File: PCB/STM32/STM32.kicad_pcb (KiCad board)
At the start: 2 copper layers, 41 x 38 mm, 47 parts, among them J18 St-Link, J2 St-Link, SW1 SW_Push, U1 LTV-356T, U2 MIC5205-5.0YM5, U3 STM32F411RETx, U4 MCP1703A-3302_SOT23, Y1 16MHz

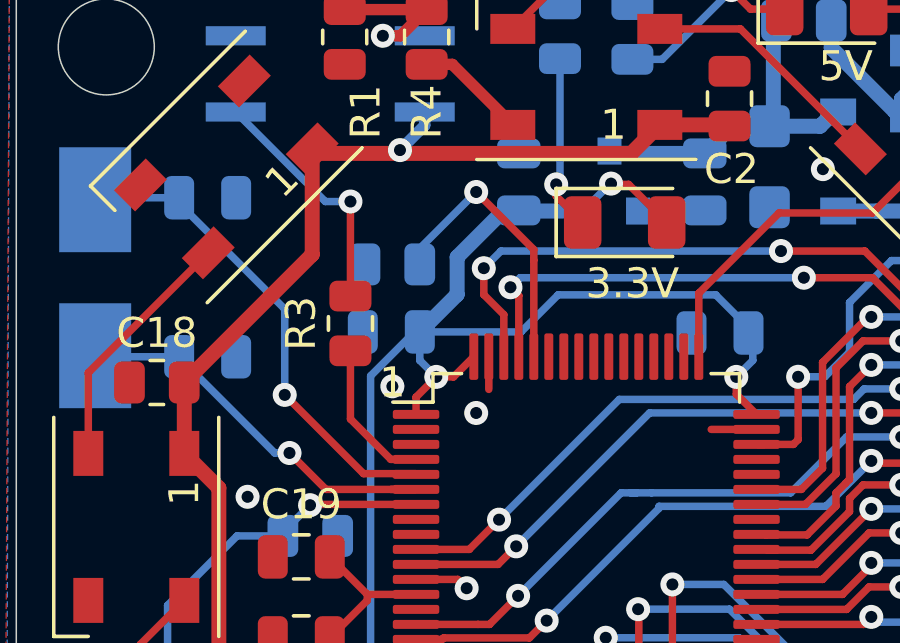
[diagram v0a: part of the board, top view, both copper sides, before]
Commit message: Changed NeoPixel output pin
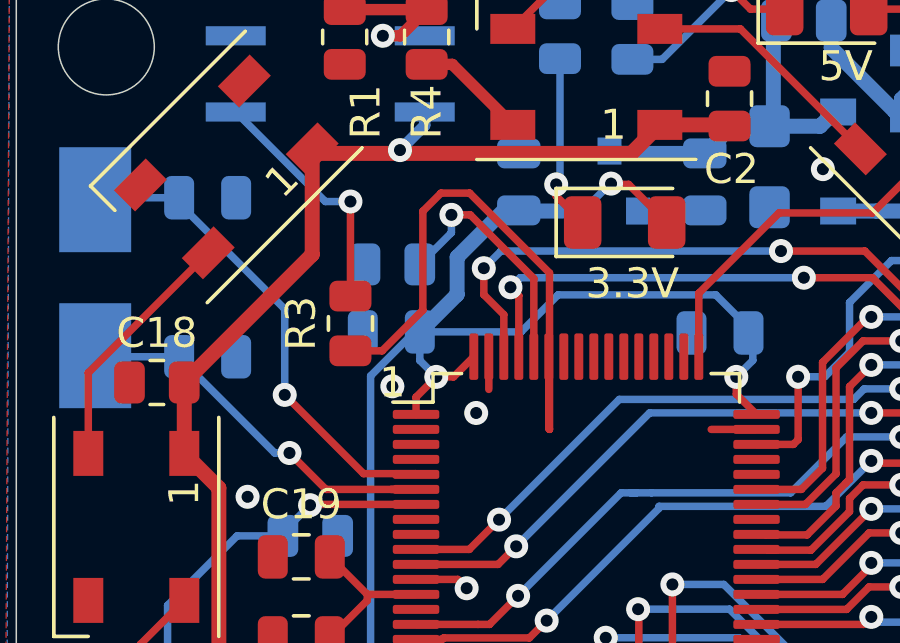
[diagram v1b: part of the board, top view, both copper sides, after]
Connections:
- R3 pad 1: PC15 -> PB7
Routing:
- net PB7: track 0.00 -> 19.5 mm
- net PC15: track 5.02 -> 0.00 mm
- net Net-(R11-Pad2): track 9.75 -> 9.13 mm

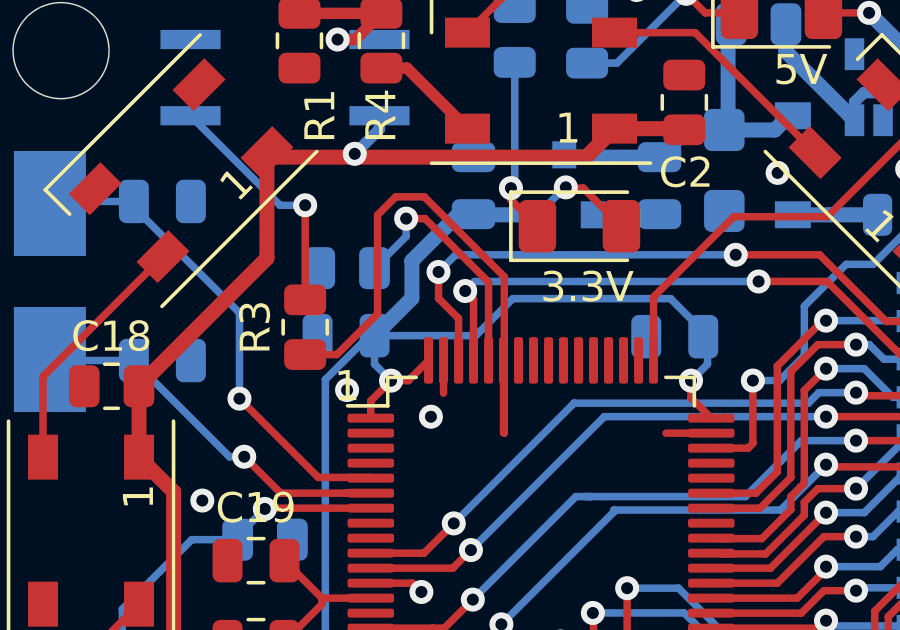
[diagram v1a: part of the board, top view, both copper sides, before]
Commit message: Changed NeoPixel output pin - fix
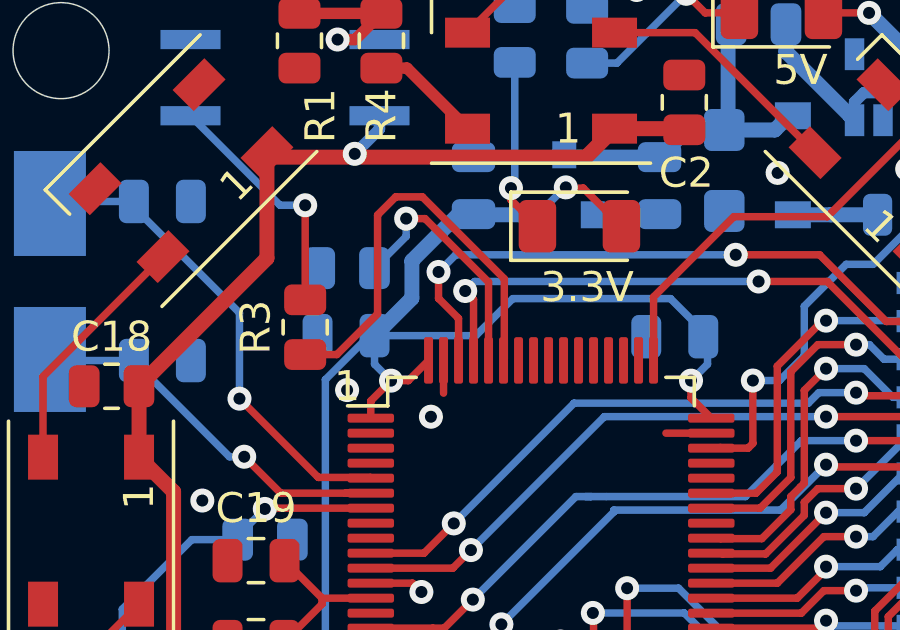
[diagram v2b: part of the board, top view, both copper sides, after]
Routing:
- net PB7: track 19.5 -> 14.6 mm

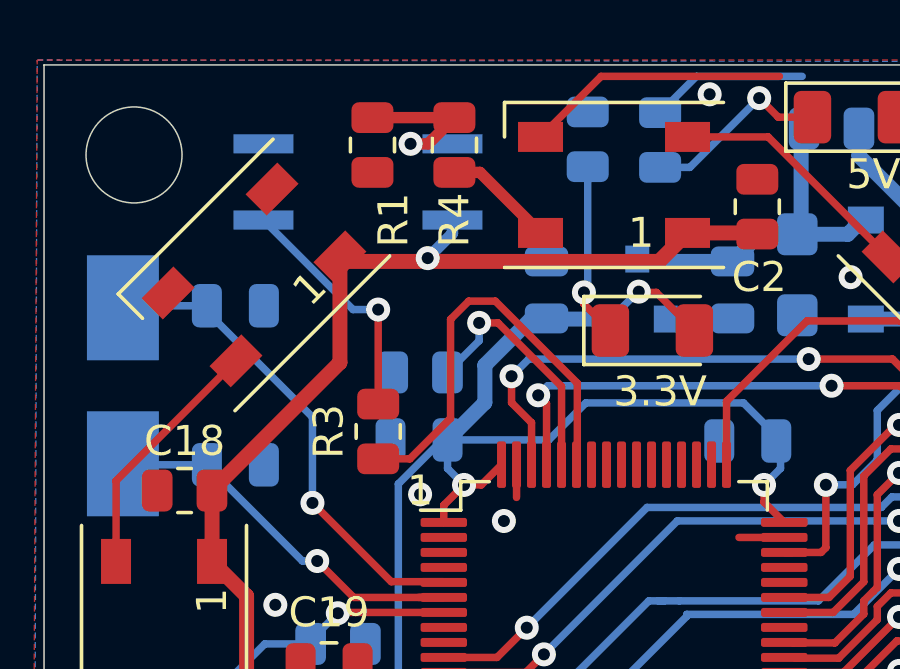
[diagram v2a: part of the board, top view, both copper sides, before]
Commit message: Added bi-directional level shifter
Replaced to newer level shifter for WS2812B
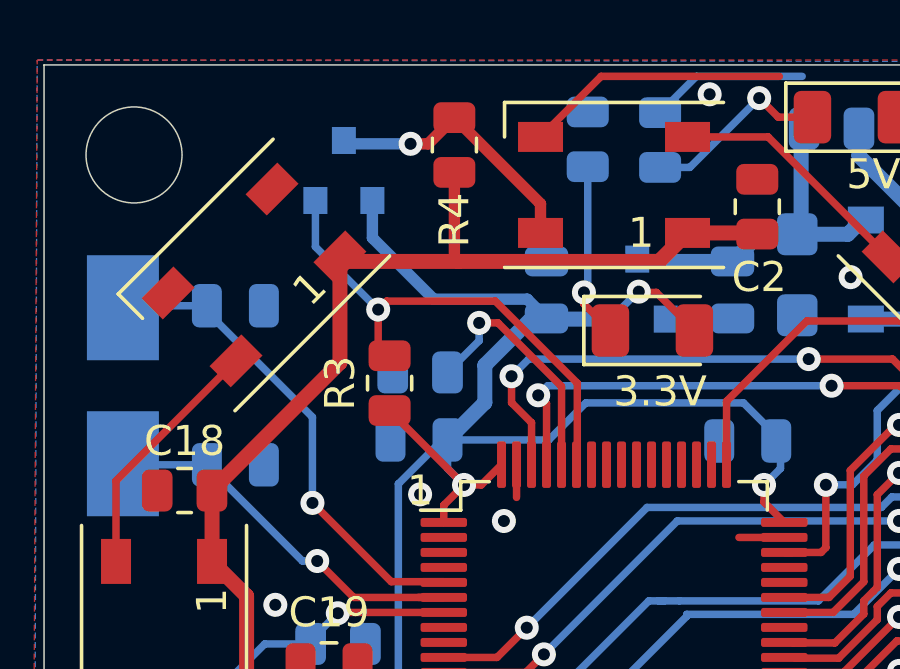
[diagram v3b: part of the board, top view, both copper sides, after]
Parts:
- removed R1: 10k, Resistor_SMD:R_0805_2012Metric
- removed U1: LTV-356T, Package_SO:SO-4_4.4x3.6mm_P2.54mm
- added Q1: BSS138, Package_TO_SOT_SMD:SOT-23, B.Cu at (91.0, 84.5)
- R3: value 220R -> 10K
- R4: value 0R -> 10K
- moved R3 1.66 mm to (92.5, 91.6)
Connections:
- R3 pad 1: PB7 -> +3V3
- R3 pad 2: Net-(R3-Pad2) -> PB7
- R4 pad 1: Net-(R1-Pad1) -> LED
- R4 pad 2: LED -> +5V
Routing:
- net +3V3: track 103.9 -> 115.6 mm
- net Net-(R3-Pad2): track 8.21 -> 0.00 mm, vias 1 -> 0
- net Net-(R1-Pad1): track 6.28 -> 0.00 mm, vias 1 -> 0
- net LED: track 3.71 -> 9.46 mm, vias 0 -> 1
- net PB7: track 14.6 -> 16.8 mm, vias 0 -> 1
- net +5V: track 130.6 -> 132.0 mm, vias 4 -> 3

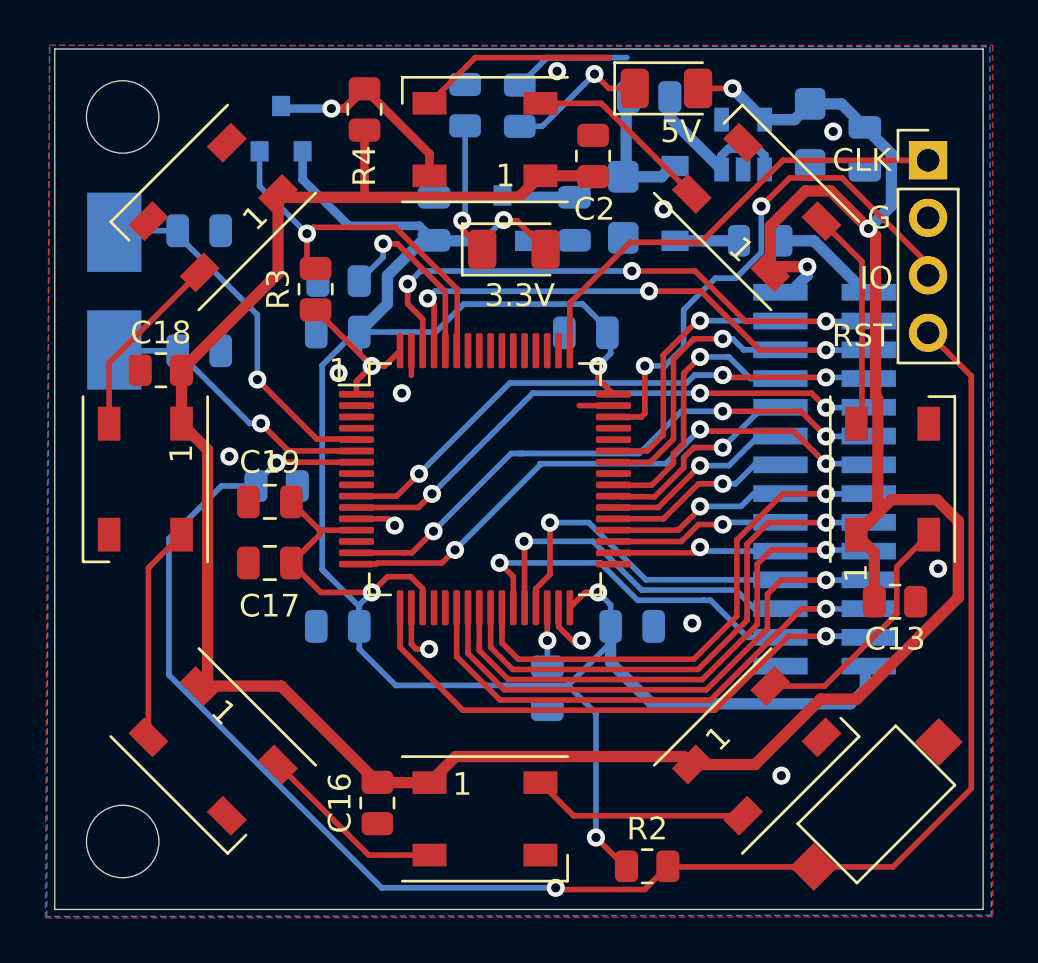
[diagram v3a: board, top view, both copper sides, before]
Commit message: Replaced 5V Power Regulator
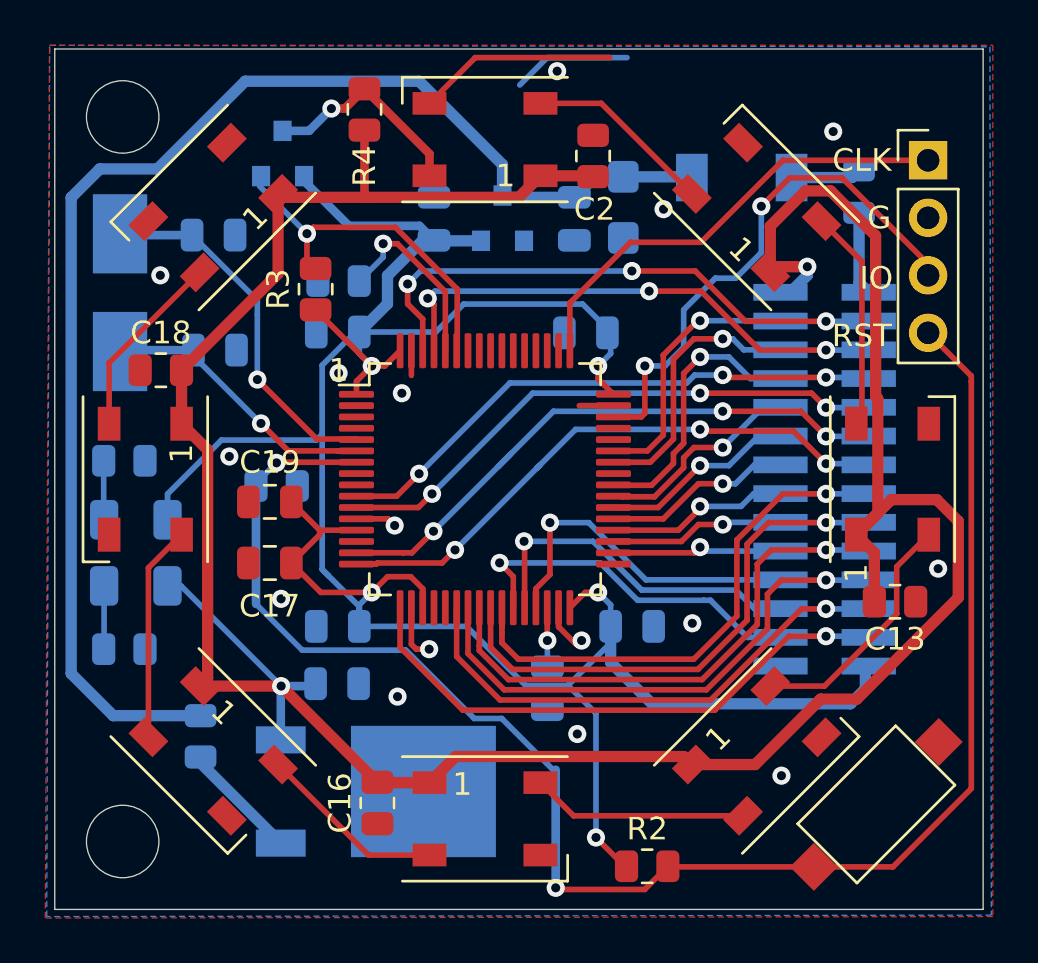
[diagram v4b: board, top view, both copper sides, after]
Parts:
- removed C3: 10uF, Capacitor_Tantalum_SMD:CP_EIA-3216-18_Kemet-A
- removed U2: MIC5205-5.0YM5, Package_TO_SOT_SMD:SOT-23-5
- added U1: L7805, Package_TO_SOT_SMD:TO-252-2, B.Cu at (95.2, 113.8)
- D1: footprint Diode_SMD:D_SOD-123 -> Diode_SMD:D_SOD-128
- D11, D2: moved to B.Cu
- moved R6 34.5 mm to (87.4, 111.4), turned to 90 degrees
- moved C14 33.2 mm to (93.5, 109.0), turned to 0 degrees
- moved D11 32.1 mm to (84.6, 104.7)
- moved R5 29.7 mm to (84.1, 107.5), turned to 0 degrees
- moved R9 21.8 mm to (84.1, 99.2), turned to 0 degrees
- moved D2 20.5 mm to (84.6, 101.8)
- moved F2 4.88 mm to (116.5, 87.3), turned to 90 degrees
- moved D1 3.16 mm to (111.3, 86.7), turned to 0 degrees
- moved Q1 1.10 mm to (91.1, 85.6)
- moved C9 0.70 mm to (88.1, 94.3)
- moved C11 0.66 mm to (88.0, 89.2)
- moved Y1 0.26 mm to (83.9, 91.8)
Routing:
- net V_Stable: track 11.7 -> 60.5 mm
- net Net-(D2-Pad1): track 6.50 -> 2.61 mm, vias 1 -> 0
- net Net-(D11-Pad1): track 6.42 -> 2.80 mm, vias 1 -> 0
- net +5V: track 132.0 -> 128.9 mm, vias 3 -> 2
- net +3V3: track 115.6 -> 118.5 mm, vias 6 -> 5
- net Net-(R6-Pad1): track 7.73 -> 5.01 mm
- net PB7: track 16.8 -> 15.3 mm
- net VPP: track 4.78 -> 3.69 mm
- net PA1: track 25.7 -> 26.3 mm
- net GND: track 23.4 -> 23.1 mm, vias 12 -> 16
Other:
- board text removed: "5V"
